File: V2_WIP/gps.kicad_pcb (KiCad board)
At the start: 6 copper layers, 82.5 x 82.5 mm, 98 parts, among them J301 USB_B_Micro, J4 BATT, J7 USB_B_Micro, Q1 IRLML5203, Q2 S8050, Q3 S8050, SW1 RotaryEncoder, SW2 MSN22AFW01, SW3 SW_Push, SW4 SW_Push, U1 ESP32-WROOM-32E, U10 24C32, U11 SN74LV1T34DBVRG4, U12 RT9742AGJ5F, U13 TP4057, U14 CH340K, U2 TPS613222ADBVR, U301 USBLC6-2SC6, U4 HT16k33, U401 NEO-M9N, U5 7seg_1x1_rgb, U6 7seg_1x1_rgb, U7 7seg_1x1_rgb, U8 KW4-804AGB, U9 TCA39306DDFR

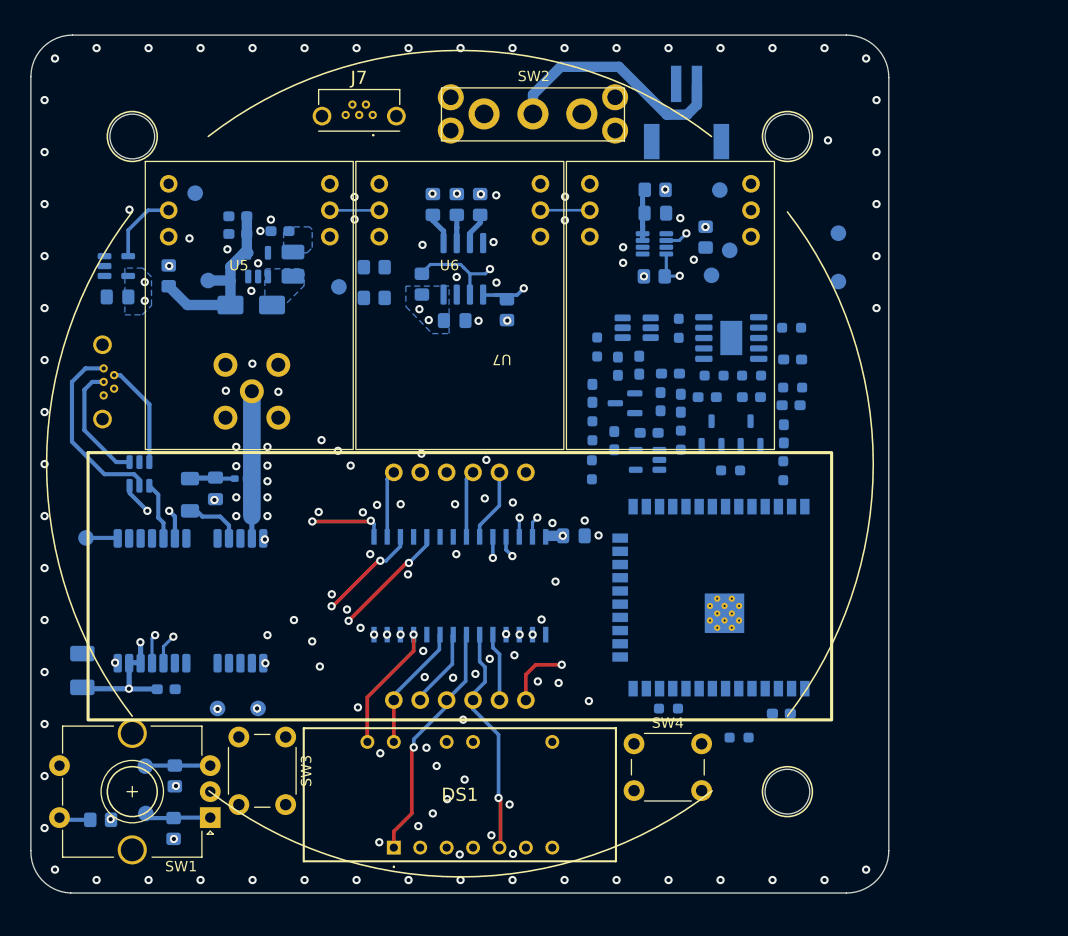
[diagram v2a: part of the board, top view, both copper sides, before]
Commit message: added LED indicators, light sensor, changed to CC 7seg displays
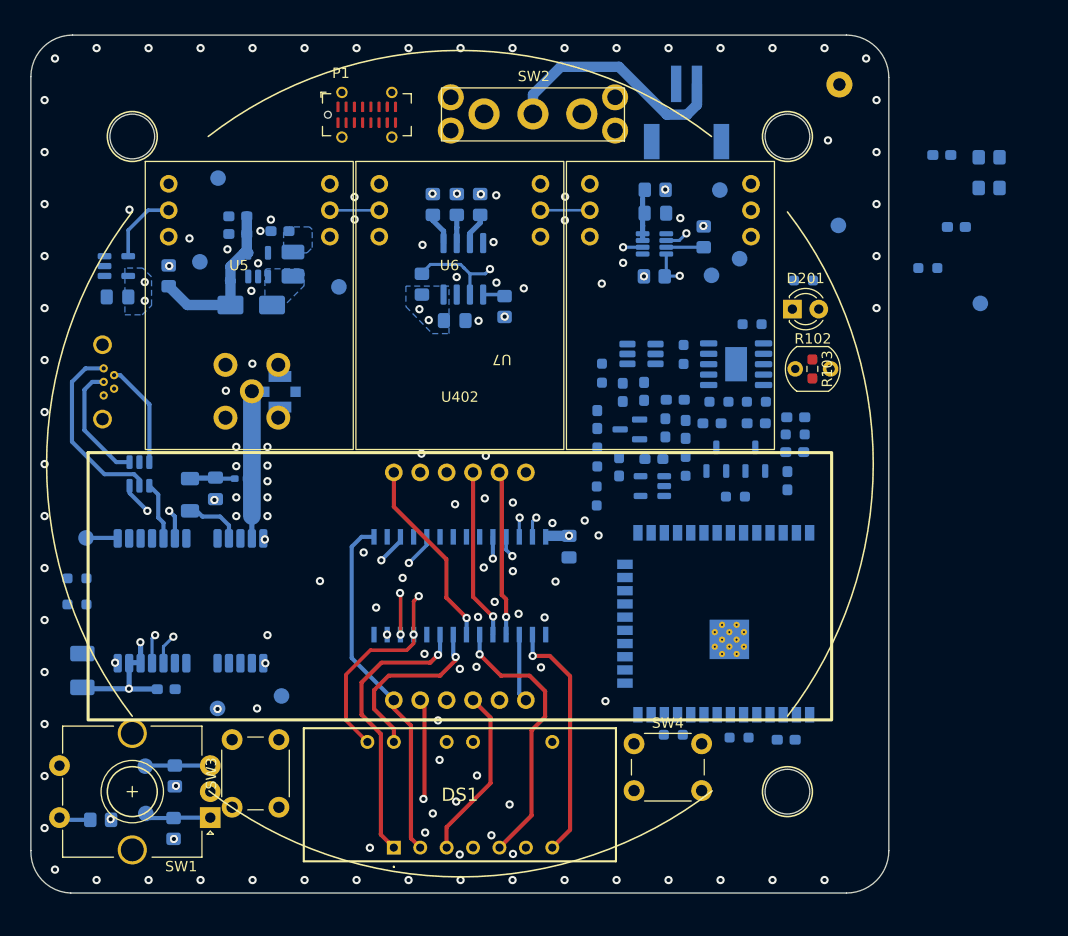
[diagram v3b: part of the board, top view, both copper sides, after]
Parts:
- removed J7: USB_B_Micro, KiCad:USB3145301A
- removed TP10: Jumper_MOSI, Resistor_SMD:R_0805_2012Metric_Pad1.20x1.40mm_HandSolder
- removed TP11: Jumper_D9, Resistor_SMD:R_0805_2012Metric_Pad1.20x1.40mm_HandSolder
- removed TP13: IO21, TestPoint:TestPoint_Pad_D1.5mm
- removed U8: KW4-804AGB, 7seg_rgb:7seg_4x1
- added AE301: Antenna_Shield, Connector_Coaxial:U.FL_Molex_MCRF_73412-0110_Vertical, B.Cu at (76.7, 76.0)
- added C101: 100n, Capacitor_SMD:C_0603_1608Metric_Pad1.08x0.95mm_HandSolder, B.Cu at (140.3, 53.3)
- added C102: 470u, Capacitor_SMD:C_0603_1608Metric_Pad1.08x0.95mm_HandSolder, B.Cu at (141.7, 60.2)
- added D201: LED, LED_THT:LED_D3.0mm, F.Cu at (126.0, 68.1)
- added P1: USB_C_Plug_USB2.0, Connector_USB:USB_C_Receptacle_G-Switch_GT-USB-7051x, F.Cu at (85.1, 49.4)
- added R102: R_Photo, OptoDevice:R_LDR_5.1x4.3mm_P3.4mm_Vertical, F.Cu at (126.2, 73.8)
- added R103: 6k, Resistor_SMD:R_0603_1608Metric_Pad0.98x0.95mm_HandSolder, F.Cu at (127.9, 73.8)
- added R104: 0R, Resistor_SMD:R_0805_2012Metric_Pad1.20x1.40mm_HandSolder, B.Cu at (144.9, 53.5)
- added R105: 0R, Resistor_SMD:R_0805_2012Metric_Pad1.20x1.40mm_HandSolder, B.Cu at (144.9, 56.5)
- added R201: 0.1, Resistor_SMD:R_0603_1608Metric_Pad0.98x0.95mm_HandSolder, B.Cu at (139.0, 64.2)
- added R301: 0R, Resistor_SMD:R_0603_1608Metric_Pad0.98x0.95mm_HandSolder, B.Cu at (57.2, 94.0)
- added R302: 0R, Resistor_SMD:R_0603_1608Metric_Pad0.98x0.95mm_HandSolder, B.Cu at (57.2, 96.5)
- added TP101: GND, TestPoint:TestPoint_THTPad_D2.5mm_Drill1.2mm, B.Cu at (130.5, 46.5)
- added TP201: FLED, TestPoint:TestPoint_Pad_D1.5mm, B.Cu at (144.1, 67.5)
- added U402: KW4-804CGB, 7seg_rgb:7seg_4x1, F.Cu at (94.0, 94.8)
- C1, C14, C15, C2: value C -> 100n
- C11, C12, C13, C3: value C -> 10u
- R10, R13, R14: value R -> 2k
- R11: value R -> 200k
- R12, R20, R9: value R -> 10k
- R15, R2: value R -> 220
- R16: value R -> 2k2
- R21: value R -> 5k1
- R7, R8: value R -> 1M
- moved R5 20.5 mm to (98.3, 67.8), turned to 90 degrees
- moved R3 20.2 mm to (117.5, 61.1), turned to -90 degrees
- moved R10 18.4 mm to (127.0, 65.3), turned to 180 degrees
- moved SW3 8.49 mm to (72.1, 116.0), turned to 90 degrees
- moved C15 5.57 mm to (126.3, 78.5)
- moved C1 4.52 mm to (126.2, 81.8)
- moved D1 4.52 mm to (125.5, 84.6)
- moved R9 4.51 mm to (126.2, 80.2)
- moved R12 3.82 mm to (122.1, 69.5), turned to 0 degrees
- moved TP403 2.63 mm to (70.8, 55.5)
- moved U12 2.56 mm to (112.5, 85.1)
- moved C11 2.56 mm to (115.7, 79.7)
- moved C12 2.56 mm to (107.2, 78.7)
- moved C13 2.56 mm to (111.7, 76.0)
- moved C14 2.56 mm to (114.7, 76.8)
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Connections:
- net /Display/aAL1 renamed /Display/a
- C11 pad 1: VCC -> /ESP/VCC
- C13 pad 1: /ESP/VUSB -> /VUSB
- C14 pad 1: /ESP/VUSB -> /VUSB
- C4 pad 1: VCC -> /VBATT
- D3 pad 1: VCC -> /ESP/VCC
- D3 pad 2: /ESP/VUSB -> /VUSB
- D4 pad 1: VCC -> /ESP/VCC
- D4 pad 2: /ESP/VUSB -> /VUSB
- D5 pad 2: /ESP/VUSB -> /VUSB
- DS1 pad 1: /Display/DPX -> /Display/CC1
- DS1 pad 6: /Display/aDP -> /Display/DPX
- J301 pad 1: Net-(J301-VBUS) -> /VUSB
- L1 pad 1: VCC -> /VBATT
- Q1 pad 1: /ESP/VUSB -> /VUSB
- Q1 pad 2: VCC -> /ESP/VCC
- R10 pad 2: Net-(D1-A) -> Net-(D201-A)
- R11 pad 1: VCC -> /ESP/VCC
- R12 pad 2: /ESP/VUSB -> /VUSB
- R7 pad 1: Net-(R7-Pad1) -> /ESP/IO34/A2
- R8 pad 2: Net-(R7-Pad1) -> /ESP/IO34/A2
- TP1 pad 1: /SDA_ESP -> /ESP/IO21/SDA
- TP2 pad 1: /SCL_ESP -> /ESP/IO22/SCL
- U1 pad 7: /ESP/IO35/A3 -> /LIGHT_SENS
- U12 pad 5: VCC -> /ESP/VCC
- U13 pad 4: /ESP/VUSB -> Net-(U13-V_{CC})
- U14 pad 7: /ESP/VUSB -> /VUSB
- U301 pad 5: Net-(J301-VBUS) -> /VUSB
- U4 pad 14: /Display/aDP -> unconnected-(U4-ROW11/K9-Pad14)
- U4 pad 16: /Display/CA1 -> unconnected-(U4-ROW9/K7-Pad16)
- U4 pad 22: /Display/CA2 -> unconnected-(U4-ROW3/K1-Pad22)
- U4 pad 23: /Display/CA3 -> unconnected-(U4-ROW2/A0-Pad23)
- U4 pad 24: /Display/CA4 -> /Display/DPX
- U4 pad 3: /Display/f -> /Display/CC44
- U4 pad 4: /Display/b -> /Display/CC33
- U4 pad 5: /Display/g -> /Display/CC22
- U4 pad 7: /Display/DPX -> /Display/CC11
- U4 pad 8: /Display/d -> /Display/L123
- U4 pad 9: /Display/L123 -> /Display/CC1
- U401 pad 22: +3V3 -> Net-(U401-V_BCKP)
- U401 pad 7: unconnected-(U401-VDD_USB-Pad7) -> Net-(U401-VDD_USB)
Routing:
- net /Display/b: track 54.3 -> 0.00 mm, vias 1 -> 0
- net (no net): track 45.3 -> 0.00 mm, vias 3 -> 1
- net /Display/f: track 43.9 -> 0.00 mm, vias 1 -> 0
- net /Display/aDP: track 37.6 -> 0.00 mm, vias 1 -> 0
- net /Display/CC3: track 59.9 -> 23.7 mm
- net /Display/CC1: track 0.00 -> 27.6 mm, vias 0 -> 1
- net /Display/CA4: track 21.3 -> 0.00 mm, vias 2 -> 0
- net /Display/aF: track 12.7 -> 33.3 mm, vias 1 -> 2
- net /Display/aBL2: track 30.6 -> 50.5 mm
- net /Display/CC11: track 0.00 -> 18.5 mm, vias 0 -> 1
- net Net-(J301-VBUS): track 18.0 -> 0.00 mm
- net /VUSB: track 0.00 -> 18.0 mm
- net /Display/CC22: track 0.00 -> 16.6 mm, vias 0 -> 1
- net /Display/CC33: track 0.00 -> 15.9 mm, vias 0 -> 1
- net /Display/aE: track 49.9 -> 34.2 mm, vias 2 -> 0
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- added copper zone on B.Cu, net /VBATT
- removed copper zone on B.Cu, net VCC
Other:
- board text added: "+5V"
- board text added: "FLED"
- board text added: "GND"
- board text added: "IO22"
- board text added: "RGB_3V3"
- board text added: "RGB_5V"
- board text added: "RXD_G"
- board text added: "SB_N"
- board text added: "SCL"
- board text added: "SDA"
- board text added: "TXD_G"

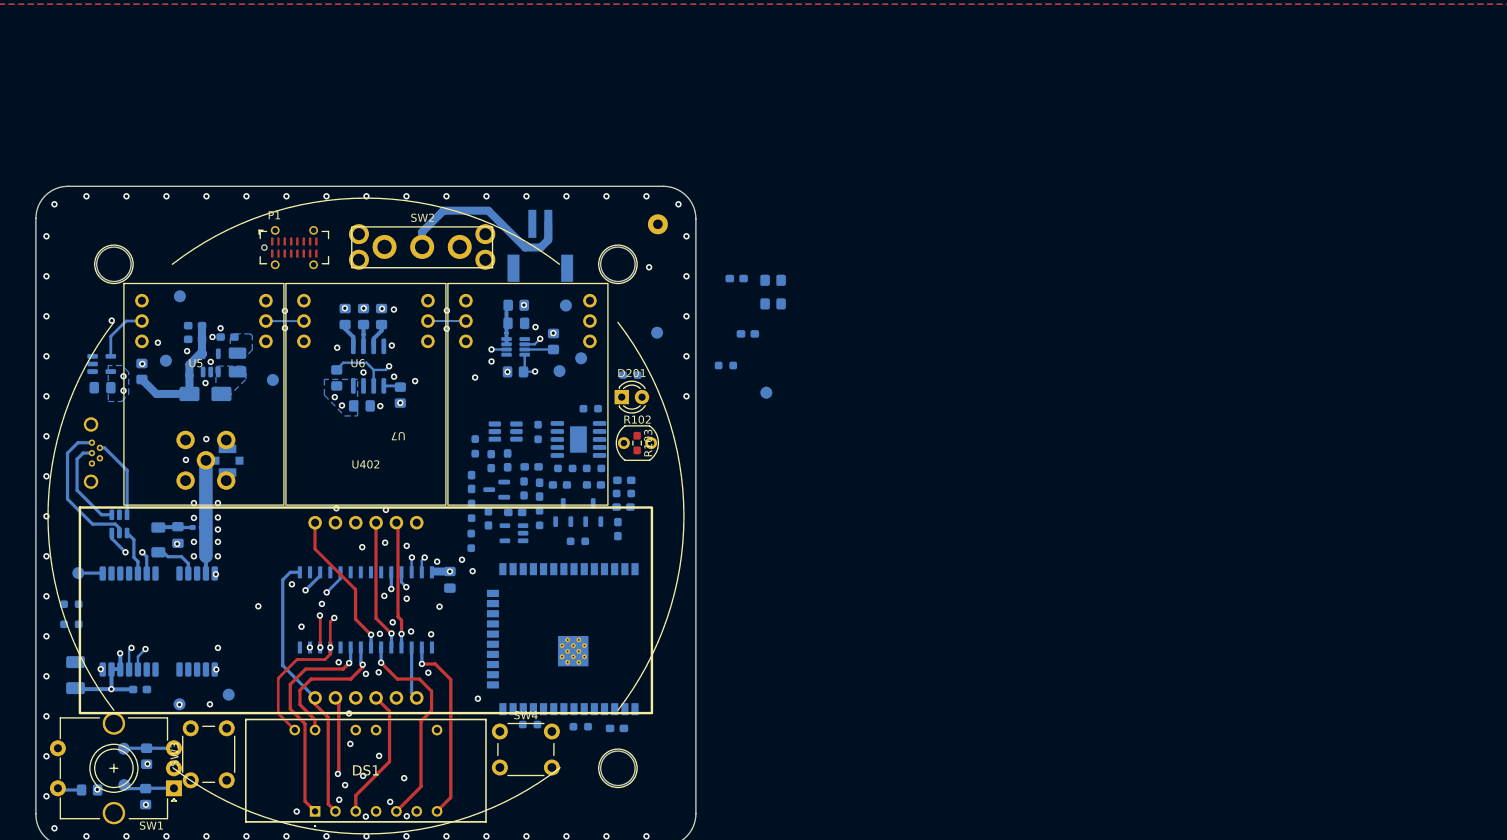
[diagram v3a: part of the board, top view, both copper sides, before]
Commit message: added battery monitoring circuits
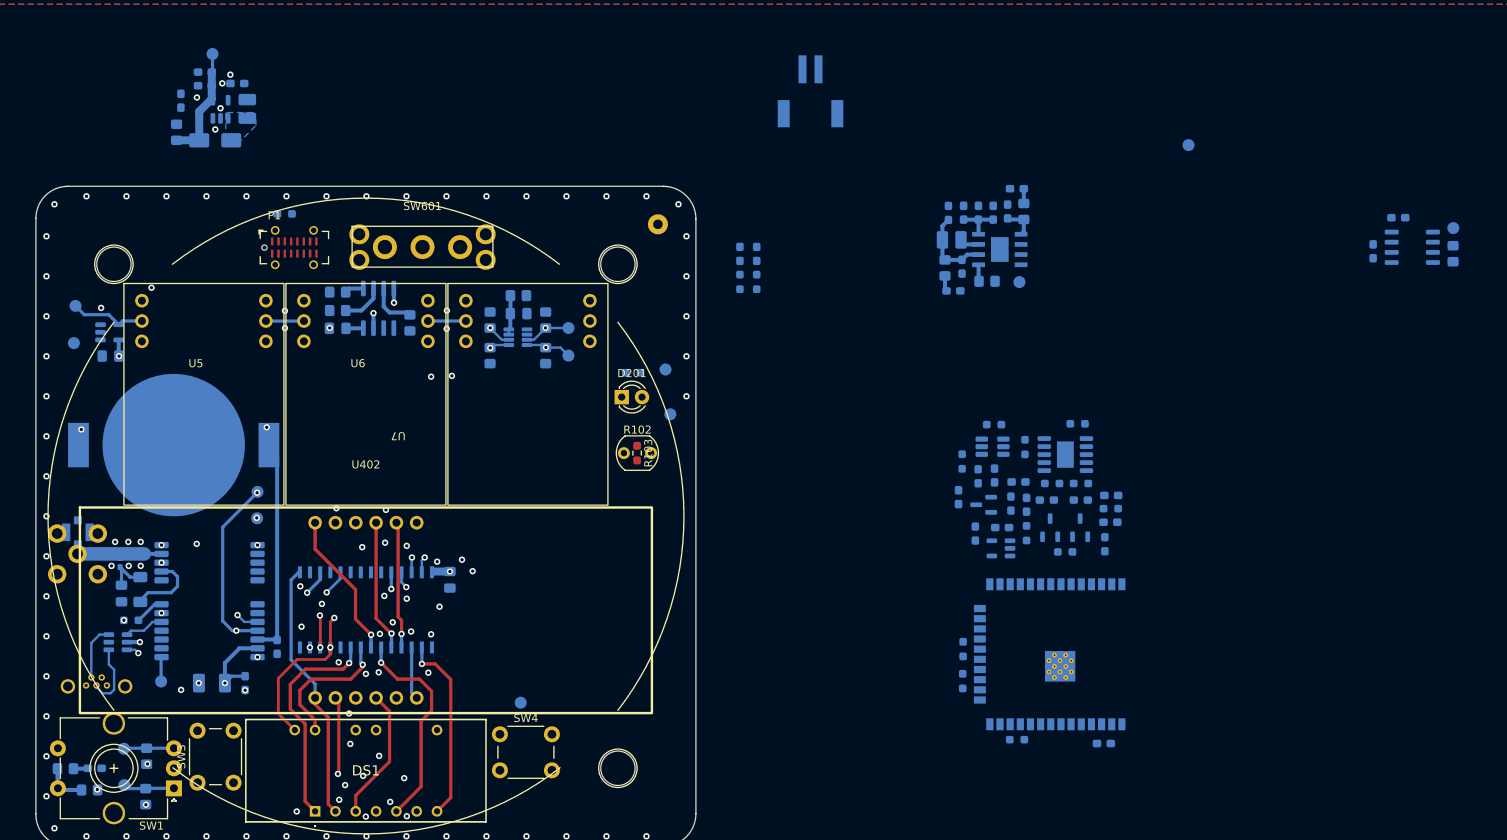
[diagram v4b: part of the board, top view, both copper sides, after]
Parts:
- removed J4: BATT, 1769:1769
- removed R302: 0R, Resistor_SMD:R_0603_1608Metric_Pad0.98x0.95mm_HandSolder
- removed R7, R8: 1M, Resistor_SMD:R_0603_1608Metric_Pad0.98x0.95mm_HandSolder
- removed SW2: MSN22AFW01, Button_Switch_THT:MSN22AFW01
- added BT301: Battery, Battery:BatteryHolder_MPD_BC2003_1x2032, B.Cu at (70.0, 74.1)
- added C301: 1uF, Capacitor_SMD:C_0603_1608Metric_Pad1.08x0.95mm_HandSolder, B.Cu at (82.9, 99.3)
- added C601: 10u, Capacitor_SMD:C_0603_1608Metric_Pad1.08x0.95mm_HandSolder, B.Cu at (174.2, 44.9)
- added C602: 10u, Capacitor_SMD:C_0603_1608Metric_Pad1.08x0.95mm_HandSolder, B.Cu at (175.4, 42.0)
- added C603: 10u, Capacitor_SMD:C_0603_1608Metric_Pad1.08x0.95mm_HandSolder, B.Cu at (168.5, 51.8)
- added C604: 10u, Capacitor_SMD:C_0603_1608Metric_Pad1.08x0.95mm_HandSolder, B.Cu at (167.4, 54.8)
- added C605: 22u, Capacitor_SMD:C_0603_1608Metric_Pad1.08x0.95mm_HandSolder, B.Cu at (168.7, 45.0)
- added C606: 22u, Capacitor_SMD:C_0603_1608Metric_Pad1.08x0.95mm_HandSolder, B.Cu at (170.6, 45.0)
- added C607: 22u, Capacitor_SMD:C_0603_1608Metric_Pad1.08x0.95mm_HandSolder, B.Cu at (172.4, 45.0)
- added C608: 100n, Capacitor_SMD:C_0603_1608Metric_Pad1.08x0.95mm_HandSolder, B.Cu at (219.9, 49.9)
- added C609: 100n, Capacitor_SMD:C_0603_1608Metric_Pad1.08x0.95mm_HandSolder, B.Cu at (223.1, 45.7)
- added D101: LED, Diode_SMD:D_0603_1608Metric_Pad1.05x0.95mm_HandSolder, B.Cu at (140.8, 50.2)
- added D102: LED, Diode_SMD:D_0603_1608Metric_Pad1.05x0.95mm_HandSolder, B.Cu at (142.8, 50.2)
- added D601: D, Diode_SMD:D_0603_1608Metric_Pad1.05x0.95mm_HandSolder, B.Cu at (166.8, 45.1)
- added J601: BATT, 1769:1769, B.Cu at (149.6, 27.1)
- added L601: 1uH, Inductor_SMD:L_1008_2520Metric_Pad1.43x2.20mm_HandSolder, B.Cu at (167.2, 48.5)
- added R101: 2k, Resistor_SMD:R_0603_1608Metric_Pad0.98x0.95mm_HandSolder, B.Cu at (140.8, 53.7)
- added R106: 2k, Resistor_SMD:R_0603_1608Metric_Pad0.98x0.95mm_HandSolder, B.Cu at (142.8, 53.7)
- added R_E101: 1k, Resistor_SMD:R_0805_2012Metric_Pad1.20x1.40mm_HandSolder, B.Cu at (56.5, 114.5)
- added R_E601: 10k, Resistor_SMD:R_0805_2012Metric_Pad1.20x1.40mm_HandSolder, B.Cu at (171.6, 53.6)
- added R_E602: 2R, Resistor_SMD:R_0805_2012Metric_Pad1.20x1.40mm_HandSolder, B.Cu at (176.2, 44.9)
- added R_E603: 2R, Resistor_SMD:R_0805_2012Metric_Pad1.20x1.40mm_HandSolder, B.Cu at (166.4, 52.0)
- added R_E604: 200k, Resistor_SMD:R_0805_2012Metric_Pad1.20x1.40mm_HandSolder, B.Cu at (229.9, 50.2)
- added SW601: MSN22AFW01, Button_Switch_THT:MSN22AFW01, F.Cu at (101.1, 44.8)
- added TP601: LED_3, TestPoint:TestPoint_Pad_D1.5mm, B.Cu at (175.7, 53.7)
- added TP602: IO0, TestPoint:TestPoint_Pad_D1.5mm, B.Cu at (229.9, 47.0)
- added TP603: +5V, TestPoint:TestPoint_Pad_D1.5mm, B.Cu at (196.8, 36.6)
- added U601: IP5306, Package_SO:SOP-8L, B.Cu at (173.2, 49.6)
- added U602: STC3100IST, Package_SO:SO-8_3.9x4.9mm_P1.27mm, B.Cu at (224.8, 49.4)
- R104, R105: footprint Resistor_SMD:R_0805_2012Metric_Pad1.20x1.40mm_HandSolder -> Resistor_SMD:R_0603_1608Metric_Pad0.98x0.95mm_HandSolder
- moved C101 100.9 mm to (60.1, 114.5), turned to 0 degrees
- moved C102 76.6 mm to (70.9, 31.1), turned to 90 degrees
- moved R21 74.0 mm to (83.8, 45.2)
- moved R20 60.9 mm to (181.4, 87.5)
- moved C13 60.9 mm to (172.6, 77.9)
- moved C2 60.9 mm to (173.5, 84.4)
- moved C3 60.9 mm to (186.2, 111.4)
- moved D1 60.9 mm to (186.4, 86.5)
- moved D4 60.9 mm to (170.2, 85.2)
- moved D6 60.9 mm to (183.4, 81.0)
- moved D7 60.9 mm to (179.1, 81.0)
- moved Q1 60.9 mm to (171.2, 81.6)
- moved Q2 60.9 mm to (183.3, 84.4)
- moved Q3 60.9 mm to (179.5, 84.4)
- moved R12 60.9 mm to (183.0, 71.4)
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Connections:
- net /ESP/IO21/SDA renamed /SDA_3V3
- net /ESP/IO22/SCL renamed /SCL_3V3
- R_E3 pad 1: /SW -> Net-(R_E101-Pad1)
- SW1 pad S1: /SW -> Net-(R_E101-Pad1)
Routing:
- net Net-(BT301-+): track 0.00 -> 50.5 mm, vias 0 -> 2
- net /Display/SDA_5V: track 4.41 -> 40.0 mm
- net +3V3: track 130.5 -> 101.8 mm, vias 8 -> 6
- net Net-(J4-Pin_1): track 23.0 -> 0.00 mm
- net /Display/SCL_5V: track 53.6 -> 37.3 mm, vias 3 -> 2
- net /GNSS_RxD: track 12.4 -> 22.7 mm
- net Net-(D601-K): track 0.00 -> 9.92 mm
- net +5V: track 1.93 -> 11.8 mm, vias 11 -> 2
- net Net-(R_E101-Pad1): track 0.00 -> 5.52 mm
- net Net-(U401-VDD_USB): track 0.00 -> 3.72 mm
- net GND: track 0.00 -> 3.66 mm, vias 123 -> 115
- net Net-(AE301-A): track 14.1 -> 10.5 mm
- net Net-(J301-D+): track 11.8 -> 8.17 mm
- net Net-(J301-D-): track 10.0 -> 6.94 mm
- net Net-(U10-E2): track 3.12 -> 5.97 mm
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- removed copper zone on B.Cu, net +5V
- removed copper zone on B.Cu, net /VBATT
